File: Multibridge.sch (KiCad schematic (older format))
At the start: 18 parts

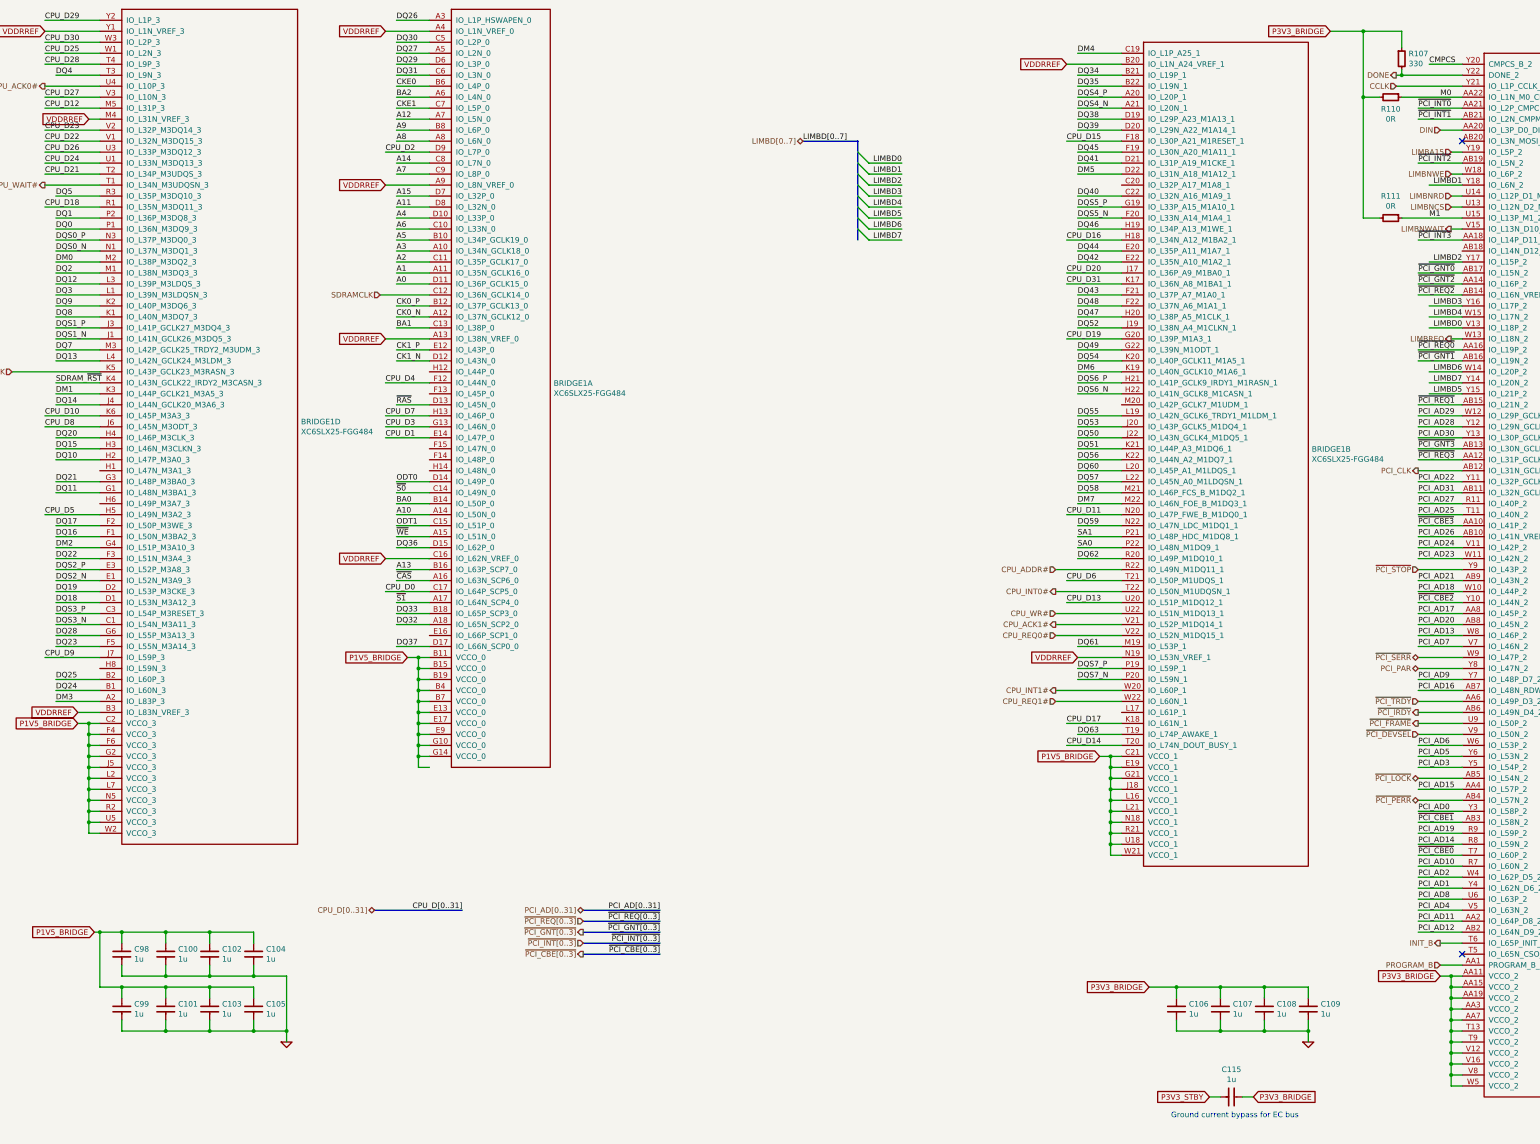
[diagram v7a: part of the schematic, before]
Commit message: Tidy up Power Distribution page
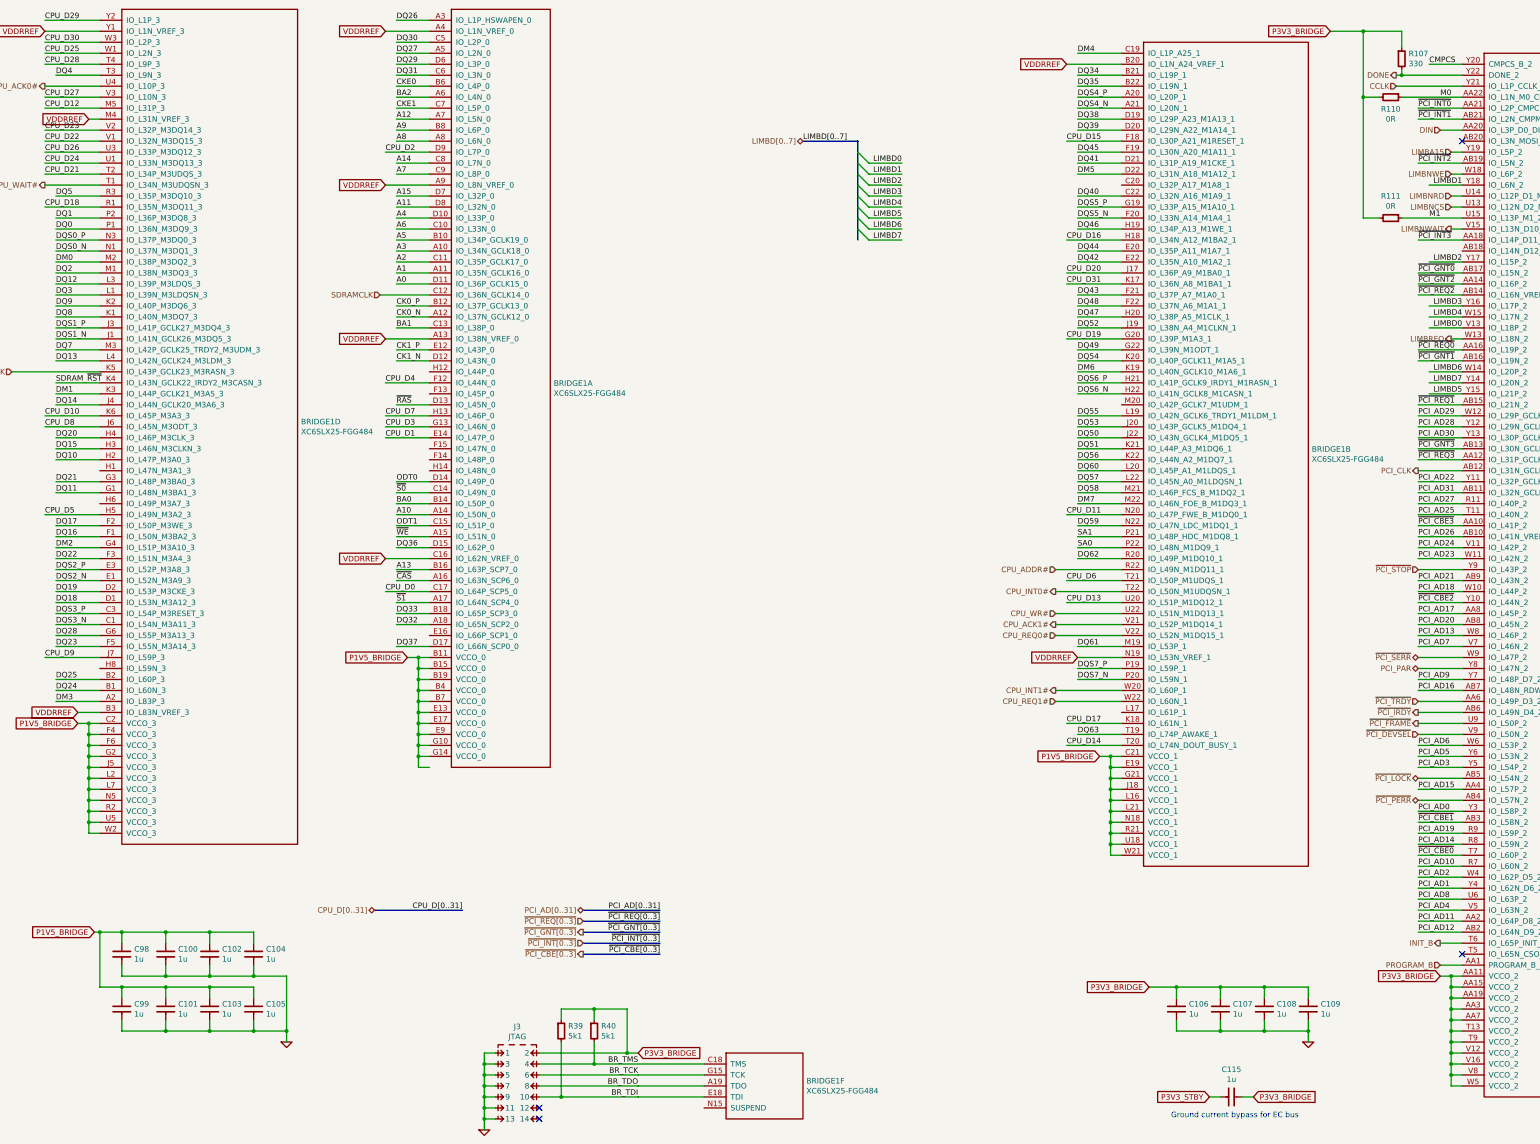
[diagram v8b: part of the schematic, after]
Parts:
- added unit 6 of BRIDGE1
- added J3: JTAG, conn-fci:98424-G52-14ALF, symbol CONN-100MIL-M-2x7-SHROUD
- added R39, R40: 5k1, IPC7351-Nominal:RESC1005X40, symbol R-0402
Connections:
- net labels added: BR_TCK, BR_TDI, BR_TDO, BR_TMS
- wire segments 474 -> 568
- no-connect marks 2 -> 4
